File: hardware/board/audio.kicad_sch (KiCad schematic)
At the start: 57 parts, among them J201 LineOut, J202 Headphone, J203 LineIn, T201 TerminalL, T202 TerminalR, U201 MAX98089ETN_T, U202 TPS7A2018PDBVR, Y201 12.288MHz

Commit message: proper audio clock LCSC
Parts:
- Y201: LCSC C20617595 -> C255992
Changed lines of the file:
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@@
 			)
 		)
-		(property "LCSC" "C20617595"
+		(property "LCSC" "C255992"
 			(at 59.69 45.72 0)
 			(hide yes)

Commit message: 1a speaker beads
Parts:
- FB202, FB203, FB204, FB205: value 600Ohm@100MHz -> 600Ohm@100MHz, 1A
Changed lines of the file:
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@@
 		(in_pos_files yes)
 		(dnp no)
-		(fields_autoplaced yes)
 		(property "Reference" "#PWR0231"
 			(at 241.3 119.38 0)
@@
 		)
 		(property "Value" "GND"
-			(at 241.3 118.11 0)
+			(at 244.348 115.062 0)
 			(show_name no)
 			(do_not_autoplace no)
@@
 			)
 		)
-		(property "Value" "600Ohm@100MHz"
+		(property "Value" "600Ohm@100MHz, 1A"
 			(at 231.1019 80.01 90)
 			(show_name no)
@@
 			)
 		)
-		(property "Value" "600Ohm@100MHz"
+		(property "Value" "600Ohm@100MHz, 1A"
 			(at 231.1019 118.11 90)
 			(show_name no)
@@
 		(in_pos_files yes)
 		(dnp no)
-		(fields_autoplaced yes)
 		(property "Reference" "#PWR0220"
 			(at 241.3 81.28 0)
@@
 		)
 		(property "Value" "GND"
-			(at 241.3 80.01 0)
+			(at 244.602 76.962 0)
 			(show_name no)
 			(do_not_autoplace no)
@@
 			)
 		)
-		(property "Value" "600Ohm@100MHz"
+		(property "Value" "600Ohm@100MHz, 1A"
 			(at 229.8319 66.04 90)
 			(show_name no)
@@
 			)
 		)
-		(property "Value" "600Ohm@100MHz"
+		(property "Value" "600Ohm@100MHz, 1A"
 			(at 231.1019 104.14 90)
 			(show_name no)

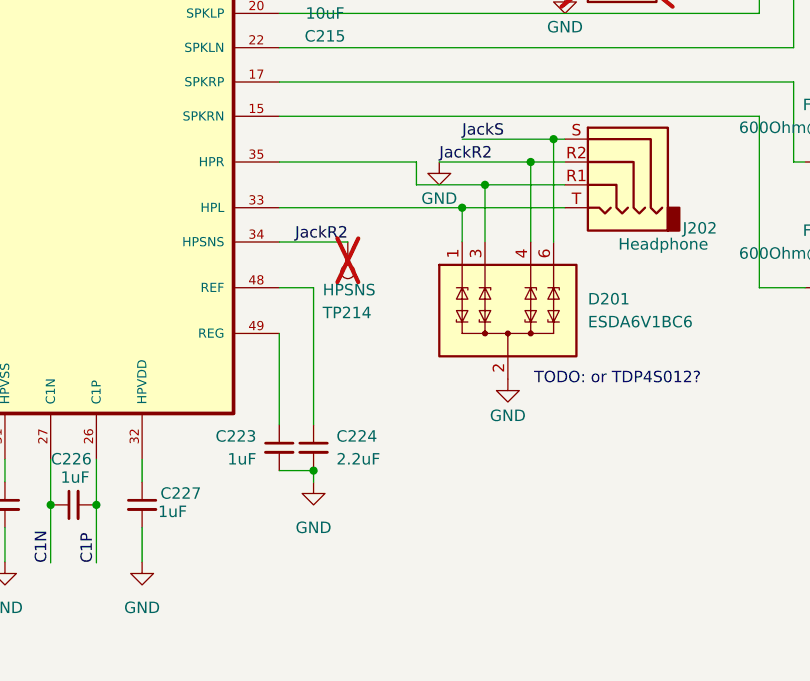
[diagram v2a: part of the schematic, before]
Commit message: wip netTie on HPSNS
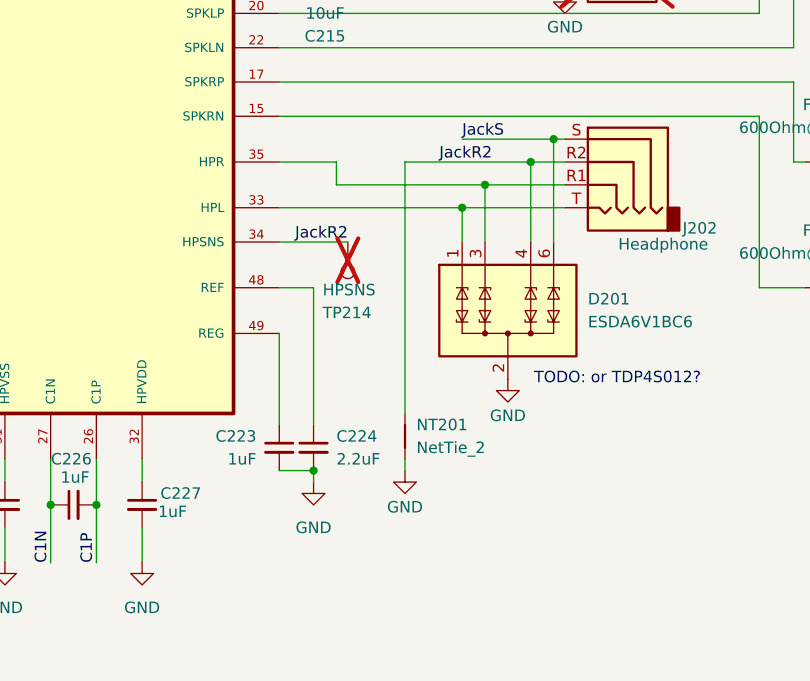
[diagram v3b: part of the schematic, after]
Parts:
- added NT201: NetTie_2, NetTie:NetTie-2_SMD_Pad0.5mm, symbol Device:NetTie_2
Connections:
- net GND: now also NT201.1; no longer C218.1, D201.4 (TVS3), J202.R2, TP214.1, U201.34 (HPSNS)
- new net JackR2: C218.1, D201.4 (TVS3), J202.R2, NT201.2, TP214.1, U201.34 (HPSNS)
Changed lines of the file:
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@@
 	)
 	(junction
-		(at 200.66 105.41)
-		(diameter 0)
-		(color 0 0 0 0)
-	)
-	(junction
 		(at 90.17 158.75)
 		(diameter 0)
@@
 	)
 	(junction
-		(at 198.12 107.95)
+		(at 241.3 107.95)
 		(diameter 0)
 		(color 0 0 0 0)
 	)
 	(junction
-		(at 193.04 110.49)
+		(at 121.92 140.97)
 		(diameter 0)
 		(color 0 0 0 0)
 	)
 	(junction
-		(at 241.3 107.95)
+		(at 59.69 36.83)
 		(diameter 0)
 		(color 0 0 0 0)
 	)
 	(junction
-		(at 121.92 140.97)
+		(at 200.66 105.41)
 		(diameter 0)
 		(color 0 0 0 0)
 	)
 	(junction
-		(at 59.69 36.83)
+		(at 193.04 110.49)
 		(diameter 0)
 		(color 0 0 0 0)
@@
 	)
 	(junction
-		(at 190.5 113.03)
-		(diameter 0)
-		(color 0 0 0 0)
-	)
-	(junction
 		(at 125.73 36.83)
 		(diameter 0)
@@
 	)
 	(junction
+		(at 198.12 107.95)
+		(diameter 0)
+		(color 0 0 0 0)
+	)
+	(junction
 		(at 127 140.97)
 		(diameter 0)
@@
 	)
 	(junction
+		(at 190.5 113.03)
+		(diameter 0)
+		(color 0 0 0 0)
+	)
+	(junction
 		(at 72.39 105.41)
 		(diameter 0)
@@
 	(wire
 		(pts
+			(xy 184.15 142.24) (xy 184.15 140.97)
+		)
+		(stroke
+			(width 0)
+			(type default)
+		)
+	)
+	(wire
+		(pts
 			(xy 227.33 95.25) (xy 227.33 83.82)
 		)
@@
 	(wire
 		(pts
-			(xy 187.96 107.95) (xy 198.12 107.95)
+			(xy 45.72 116.84) (xy 55.88 116.84)
 		)
 		(stroke
@@
 	(wire
 		(pts
-			(xy 45.72 116.84) (xy 55.88 116.84)
+			(xy 35.56 105.41) (xy 35.56 106.68)
 		)
 		(stroke
@@
 	(wire
 		(pts
-			(xy 35.56 105.41) (xy 35.56 106.68)
+			(xy 125.73 27.94) (xy 125.73 30.48)
 		)
 		(stroke
@@
 	(wire
 		(pts
-			(xy 125.73 27.94) (xy 125.73 30.48)
+			(xy 223.52 69.85) (xy 227.33 69.85)
 		)
 		(stroke
@@
 	(wire
 		(pts
-			(xy 223.52 69.85) (xy 227.33 69.85)
+			(xy 125.73 46.99) (xy 125.73 49.53)
 		)
 		(stroke
@@
 	(wire
 		(pts
-			(xy 125.73 46.99) (xy 125.73 49.53)
+			(xy 128.27 46.99) (xy 128.27 48.26)
 		)
 		(stroke
@@
 	(wire
 		(pts
-			(xy 128.27 46.99) (xy 128.27 48.26)
+			(xy 184.15 107.95) (xy 198.12 107.95)
 		)
 		(stroke
@@
 	(wire
 		(pts
-			(xy 193.04 110.49) (xy 185.42 110.49)
+			(xy 193.04 110.49) (xy 176.53 110.49)
 		)
 		(stroke
@@
 	(wire
 		(pts
-			(xy 185.42 110.49) (xy 185.42 107.95)
+			(xy 176.53 110.49) (xy 176.53 107.95)
 		)
 		(stroke
@@
 	(wire
 		(pts
+			(xy 184.15 107.95) (xy 184.15 135.89)
+		)
+		(stroke
+			(width 0)
+			(type default)
+		)
+	)
+	(wire
+		(pts
 			(xy 64.77 105.41) (xy 72.39 105.41)
 		)
@@
 	(wire
 		(pts
-			(xy 170.18 107.95) (xy 185.42 107.95)
+			(xy 170.18 107.95) (xy 176.53 107.95)
 		)
 		(stroke
@@
 	)
 	(symbol
+		(lib_id "Device:NetTie_2")
+		(at 184.15 138.43 90)
+		(unit 1)
+		(body_style 1)
+		(exclude_from_sim no)
+		(in_bom no)
+		(on_board yes)
+		(in_pos_files yes)
+		(dnp no)
+		(fields_autoplaced yes)
+		(property "Reference" "NT201"
+			(at 185.42 137.1599 90)
+			(show_name no)
+			(do_not_autoplace no)
+			(effects
+				(font
+					(size 1.27 1.27)
+				)
+				(justify right)
+			)
+		)
+		(property "Value" "NetTie_2"
+			(at 185.42 139.6999 90)
+			(show_name no)
+			(do_not_autoplace no)
+			(effects
+				(font
+					(size 1.27 1.27)
+				)
+				(justify right)
+			)
+		)
+		(property "Footprint" "NetTie:NetTie-2_SMD_Pad0.5mm"
+			(at 184.15 138.43 0)
+			(hide yes)
+			(show_name no)
+			(do_not_autoplace no)
+			(effects
+				(font
+					(size 1.27 1.27)
+				)
+			)
+		)
+		(property "Datasheet" ""
+			(at 184.15 138.43 0)
+			(hide yes)
+			(show_name no)
+			(do_not_autoplace no)
+			(effects
+				(font
+					(size 1.27 1.27)
+				)
+			)
+		)
+		(property "Description" "Net tie, 2 pins"
+			(at 184.15 138.43 0)
+			(hide yes)
+			(show_name no)
+			(do_not_autoplace no)
+			(effects
+				(font
+					(size 1.27 1.27)
+				)
+			)
+		)
+		(pin "2"
+		)
+		(pin "1"
+		)
+		(instances
+			(project "board"
+				(path "/dd13fd41-39ab-4435-9074-5024f1786746/bead49b4-6be4-481c-a37b-4cba7f02eadb"
+					(reference "NT201")
+					(unit 1)
+				)
+			)
+		)
+	)
+	(symbol
 		(lib_id "Connector_Audio:AudioJack4")
 		(at 207.01 107.95 0)
@@
 	)
 	(symbol
-		(lib_id "power:GND")
-		(at 187.96 107.95 0)
-		(unit 1)
-		(body_style 1)
-		(exclude_from_sim no)
-		(in_bom yes)
-		(on_board yes)
-		(in_pos_files yes)
-		(dnp no)
-		(property "Reference" "#PWR0229"
-			(at 187.96 114.3 0)
-			(hide yes)
-			(show_name no)
-			(do_not_autoplace no)
-			(effects
-				(font
-					(size 1.27 1.27)
-				)
-			)
-		)
-		(property "Value" "GND"
-			(at 187.96 112.014 0)
-			(show_name no)
-			(do_not_autoplace no)
-			(effects
-				(font
-					(size 1.27 1.27)
-				)
-			)
-		)
-		(property "Footprint" ""
-			(at 187.96 107.95 0)
-			(hide yes)
-			(show_name no)
-			(do_not_autoplace no)
-			(effects
-				(font
-					(size 1.27 1.27)
-				)
-			)
-		)
-		(property "Datasheet" ""
-			(at 187.96 107.95 0)
-			(hide yes)
-			(show_name no)
-			(do_not_autoplace no)
-			(effects
-				(font
-					(size 1.27 1.27)
-				)
-			)
-		)
-		(property "Description" "Power symbol creates a global label with name \"GND\" , ground"
-			(at 187.96 107.95 0)
-			(hide yes)
-			(show_name no)
-			(do_not_autoplace no)
-			(effects
-				(font
-					(size 1.27 1.27)
-				)
-			)
-		)
-		(pin "1"
-		)
-		(instances
-			(project "board"
-				(path "/dd13fd41-39ab-4435-9074-5024f1786746/bead49b4-6be4-481c-a37b-4cba7f02eadb"
-					(reference "#PWR0229")
-					(unit 1)
-				)
-			)
-		)
-	)
-	(symbol
 		(lib_id "Device:C_Small")
 		(at 45.72 165.1 0)
@@
 					(unit 1)
 				)
+			)
+		)
+	)
+	(symbol
+		(lib_id "power:GND")
+		(at 184.15 142.24 0)
+		(unit 1)
+		(body_style 1)
+		(exclude_from_sim no)
+		(in_bom yes)
+		(on_board yes)
+		(in_pos_files yes)
+		(dnp no)
+		(property "Reference" "#PWR0229"
+			(at 184.15 148.59 0)
+			(hide yes)
+			(show_name no)
+			(do_not_autoplace no)
+			(effects
+				(font
+					(size 1.27 1.27)
+				)
+			)
+		)
+		(property "Value" "GND"
+			(at 184.15 146.304 0)
+			(show_name no)
+			(do_not_autoplace no)
+			(effects
+				(font
+					(size 1.27 1.27)
+				)
+			)
+		)
+		(property "Footprint" ""
+			(at 184.15 142.24 0)
+			(hide yes)
+			(show_name no)
+			(do_not_autoplace no)
+			(effects
+				(font
+					(size 1.27 1.27)
+				)
+			)
+		)
+		(property "Datasheet" ""
+			(at 184.15 142.24 0)
+			(hide yes)
+			(show_name no)
+			(do_not_autoplace no)
+			(effects
+				(font
+					(size 1.27 1.27)
+				)
+			)
+		)
+		(property "Description" "Power symbol creates a global label with name \"GND\" , ground"
+			(at 184.15 142.24 0)
+			(hide yes)
+			(show_name no)
+			(do_not_autoplace no)
+			(effects
+				(font
+					(size 1.27 1.27)
+				)
+			)
+		)
+		(pin "1"
+		)
+		(instances
+			(project "board"
+				(path "/dd13fd41-39ab-4435-9074-5024f1786746/bead49b4-6be4-481c-a37b-4cba7f02eadb"
+					(reference "#PWR0229")
+					(unit 1)
+				)

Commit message: finish jackr2
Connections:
- net JACKSENSE: now also D201.4 (TVS3); no longer D201.6 (TVS4)
- net JackR2: now also D201.6 (TVS4); no longer D201.4 (TVS3)
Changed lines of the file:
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@@
+	)
+	(junction
+		(at 200.66 107.95)
+		(diameter 0)
+		(color 0 0 0 0)
 	)
 	(junction
@@
 	)
 	(junction
-		(at 200.66 105.41)
-		(diameter 0)
-		(color 0 0 0 0)
-	)
-	(junction
 		(at 193.04 110.49)
 		(diameter 0)
@@
 	)
 	(junction
-		(at 198.12 107.95)
-		(diameter 0)
-		(color 0 0 0 0)
-	)
-	(junction
 		(at 127 140.97)
 		(diameter 0)
@@
 	(junction
 		(at 144.78 146.05)
+		(diameter 0)
+		(color 0 0 0 0)
+	)
+	(junction
+		(at 198.12 105.41)
 		(diameter 0)
 		(color 0 0 0 0)
@@
 	(wire
 		(pts
+			(xy 200.66 107.95) (xy 201.93 107.95)
+		)
+		(stroke
+			(width 0)
+			(type default)
+		)
+	)
+	(wire
+		(pts
 			(xy 45.72 111.76) (xy 49.53 111.76)
 		)
@@
 	(wire
 		(pts
-			(xy 184.15 107.95) (xy 198.12 107.95)
-		)
-		(stroke
-			(width 0)
-			(type default)
-		)
-	)
-	(wire
-		(pts
 			(xy 227.33 99.06) (xy 170.18 99.06)
 		)
@@
 	(wire
 		(pts
-			(xy 190.5 105.41) (xy 200.66 105.41)
-		)
-		(stroke
-			(width 0)
-			(type default)
-		)
-	)
-	(wire
-		(pts
 			(xy 82.55 116.84) (xy 82.55 119.38)
 		)
@@
 	(wire
 		(pts
-			(xy 200.66 105.41) (xy 201.93 105.41)
+			(xy 190.5 105.41) (xy 198.12 105.41)
 		)
 		(stroke
@@
 	(wire
 		(pts
+			(xy 198.12 105.41) (xy 198.12 116.84)
+		)
+		(stroke
+			(width 0)
+			(type default)
+		)
+	)
+	(wire
+		(pts
 			(xy 233.68 121.92) (xy 255.27 121.92)
 		)
@@
 	(wire
 		(pts
-			(xy 198.12 107.95) (xy 198.12 116.84)
-		)
-		(stroke
-			(width 0)
-			(type default)
-		)
-	)
-	(wire
-		(pts
 			(xy 96.52 85.09) (xy 99.06 85.09)
 		)
@@
 	(wire
 		(pts
+			(xy 200.66 107.95) (xy 200.66 116.84)
+		)
+		(stroke
+			(width 0)
+			(type default)
+		)
+	)
+	(wire
+		(pts
 			(xy 139.7 152.4) (xy 139.7 148.59)
 		)
@@
 	(wire
 		(pts
-			(xy 198.12 107.95) (xy 201.93 107.95)
+			(xy 184.15 107.95) (xy 200.66 107.95)
 		)
 		(stroke
@@
 	(wire
 		(pts
-			(xy 200.66 105.41) (xy 200.66 116.84)
-		)
-		(stroke
-			(width 0)
-			(type default)
-		)
-	)
-	(wire
-		(pts
 			(xy 170.18 102.87) (xy 223.52 102.87)
 		)
@@
 		)
 		(stroke
+			(width 0)
+			(type default)
+		)
+	)
+	(wire
+		(pts
+			(xy 198.12 105.41) (xy 201.93 105.41)
+		)
+		(stroke

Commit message: rewrite LCSC
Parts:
- C205, C206, C207, C208, C209, C217, C218, C220, C221, C223, C225, C226, C227, C228, C229, CX201: LCSC C28323 -> C376926; MPN (none) -> TCC0805X7R105K500DT; Manufacturer (none) -> CCTC
- FB202, FB203, FB204, FB205: LCSC C341663 -> C41556732; MPN (none) -> BLM21PG601SN1D; Manufacturer (none) -> Murata
- LS201, LS202: LCSC C474881 -> (none)
- U202: MPN (none) -> TPS7A2018PDBVR; Manufacturer (none) -> Texas Instruments
- Y201: MPN (none) -> X1G0041710019; Manufacturer (none) -> EPSON
